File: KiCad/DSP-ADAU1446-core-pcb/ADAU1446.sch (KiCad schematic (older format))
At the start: 4 parts

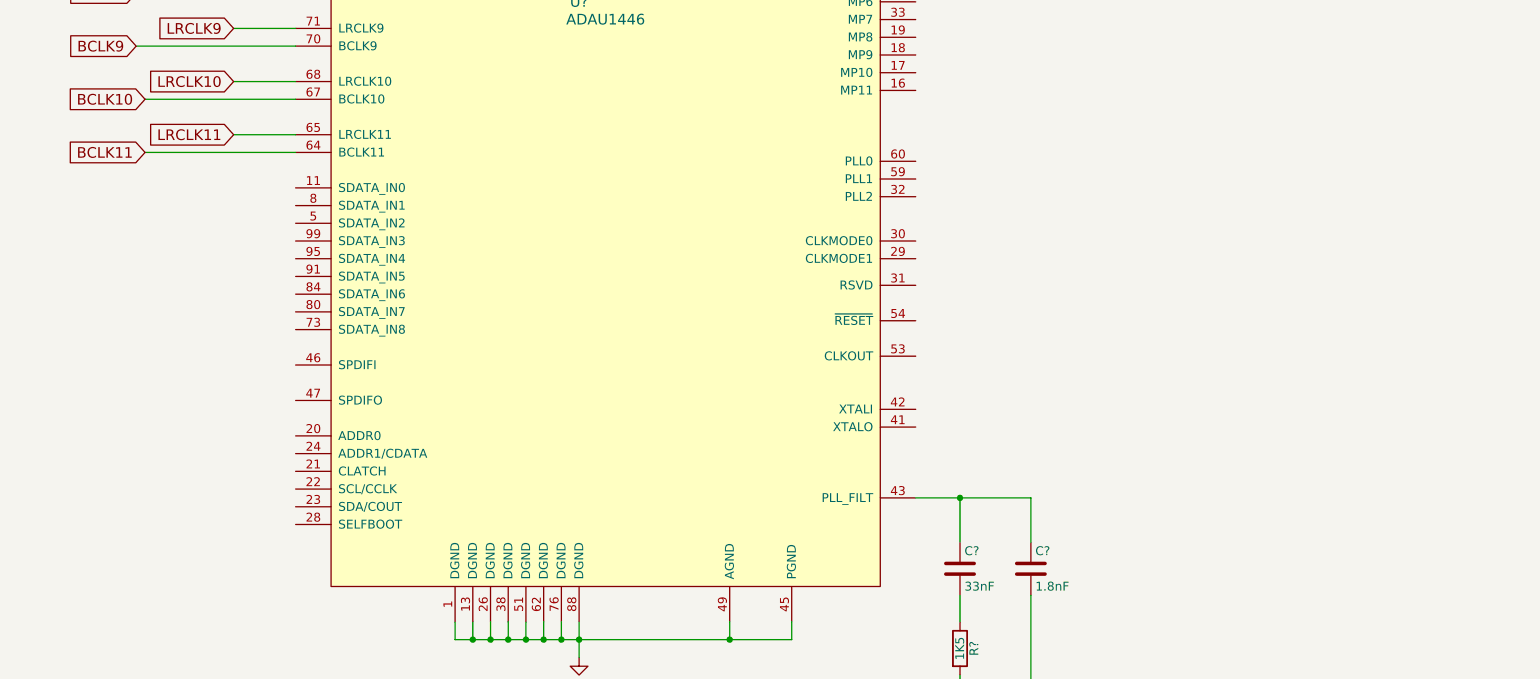
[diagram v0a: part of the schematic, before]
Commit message: - added switches library - updated ADAU1446 DSP core schematic
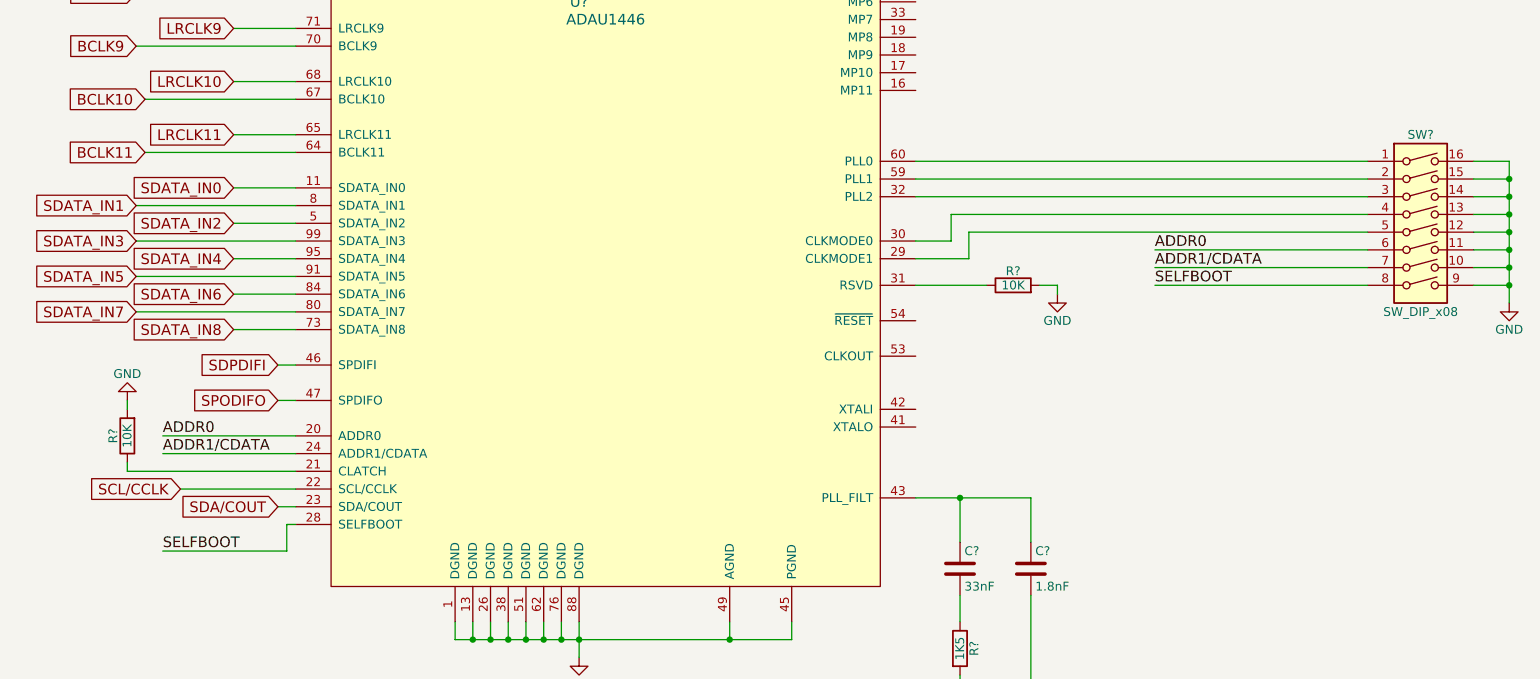
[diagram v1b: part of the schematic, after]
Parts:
- added R? (x2): 10K, symbol R
- added SW?: SW_DIP_x08, symbol SW_DIP_x08
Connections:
- net GND: now also R?.2, R?.2, SW?.10, SW?.11, SW?.12, SW?.13, SW?.14, SW?.15, SW?.16, SW?.9
- net SDATA_IN0: now reaches U?.11 (SDATA_IN0)
- net ADDR0: now reaches U?.20 (ADDR0)
- net ADDR0: now also SW?.6
- net at U?.21 (CLATCH): now also R?.1
- net SCL/CCLK: now reaches U?.22 (SCL/CCLK)
- net SDA/COUT: now reaches U?.23 (SDA/COUT)
- net ADDR1/CDATA: now reaches U?.24 (ADDR1/CDATA)
- net ADDR1/CDATA: now also SW?.7
- net SELFBOOT: now reaches U?.28 (SELFBOOT)
- net SELFBOOT: now also SW?.8
- net at U?.29 (CLKMODE1): now also SW?.5
- net at U?.30 (CLKMODE0): now also SW?.4
- net at U?.31 (RSVD): now also R?.1
- net at U?.32 (PLL2): now also SW?.3
- net SDPDIFI: now reaches U?.46 (SPDIFI)
- net SPODIFO: now reaches U?.47 (SPDIFO)
- net SDATA_IN2: now reaches U?.5 (SDATA_IN2)
- net at U?.59 (PLL1): now also SW?.2
- net at U?.60 (PLL0): now also SW?.1
- net SDATA_IN8: now reaches U?.73 (SDATA_IN8)
- net SDATA_IN1: now reaches U?.8 (SDATA_IN1)
- net SDATA_IN7: now reaches U?.80 (SDATA_IN7)
- net SDATA_IN6: now reaches U?.84 (SDATA_IN6)
- net SDATA_IN5: now reaches U?.91 (SDATA_IN5)
- net SDATA_IN4: now reaches U?.95 (SDATA_IN4)
- net SDATA_IN3: now reaches U?.99 (SDATA_IN3)
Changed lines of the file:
@@
 LIBS:valves
 LIBS:DSP-ADAU1446-core-pcb-cache
+LIBS:switches
 EELAYER 25 0
 EELAYER END
@@
 Wire Wire Line
 	10100 4300 9600 4300
+$Comp
+L SW_DIP_x08 SW?
+U 1 1 588F2B4E
+P 12450 6550
+F 0 "SW?" H 12450 7100 50  0000 C CNN
+F 1 "SW_DIP_x08" H 12450 6100 50  0000 C CNN
+F 2 "" H 12450 6550 50  0000 C CNN
+F 3 "" H 12450 6550 50  0000 C CNN
+	1    12450 6550
+	1    0    0    -1
+$EndComp
+$Comp
+L GND #PWR?
+U 1 1 588F2C1E
+P 12950 6950
+F 0 "#PWR?" H 12950 6700 50  0001 C CNN
+F 1 "GND" H 12950 6800 50  0000 C CNN
+F 2 "" H 12950 6950 50  0000 C CNN
+F 3 "" H 12950 6950 50  0000 C CNN
+	1    12950 6950
+	1    0    0    -1
+$EndComp
+Wire Wire Line
+	12750 6150 12950 6150
+Wire Wire Line
+	12950 6150 12950 6950
+Wire Wire Line
+	12750 6850 12950 6850
+Connection ~ 12950 6850
+Wire Wire Line
+	12750 6750 12950 6750
+Connection ~ 12950 6750
+Wire Wire Line
+	12750 6650 12950 6650
+Connection ~ 12950 6650
+Wire Wire Line
+	12750 6550 12950 6550
+Connection ~ 12950 6550
+Wire Wire Line
+	12750 6450 12950 6450
+Connection ~ 12950 6450
+Wire Wire Line
+	12750 6350 12950 6350
+Connection ~ 12950 6350
+Wire Wire Line
+	12750 6250 12950 6250
+Connection ~ 12950 6250
+Wire Wire Line
+	9600 6150 12150 6150
+Wire Wire Line
+	9600 6250 12150 6250
+Wire Wire Line
+	9600 6350 12150 6350
+Wire Wire Line
+	9600 6600 9800 6600
+Wire Wire Line
+	9800 6600 9800 6450
+Wire Wire Line
+	9800 6450 12150 6450
+Wire Wire Line
+	9600 6700 9900 6700
+Wire Wire Line
+	9900 6700 9900 6550
+Wire Wire Line
+	9900 6550 12150 6550
+Text Label 10950 6850 0    60   ~ 0
+SELFBOOT
+Wire Wire Line
+	10950 6850 12150 6850
+Text Label 10950 6650 0    60   ~ 0
+ADDR0
+Text Label 10950 6750 0    60   ~ 0
+ADDR1/CDATA
+Wire Wire Line
+	10950 6650 12150 6650
+Wire Wire Line
+	10950 6750 12150 6750
+Text Label 5350 7700 0    60   ~ 0
+ADDR0
+Text Label 5350 7800 0    60   ~ 0
+ADDR1/CDATA
+Text Label 5350 8350 0    60   ~ 0
+SELFBOOT
+Wire Wire Line
+	6100 7800 5350 7800
+Wire Wire Line
+	6100 7700 5350 7700
+$Comp
+L R R?
+U 1 1 588F383C
+P 10150 6850
+F 0 "R?" V 10230 6850 50  0000 C CNN
+F 1 "10K" V 10150 6850 50  0000 C CNN
+F 2 "" V 10080 6850 50  0000 C CNN
+F 3 "" H 10150 6850 50  0000 C CNN
+	1    10150 6850
+	0    -1   -1   0
+$EndComp
+Wire Wire Line
+	9600 6850 10000 6850
+$Comp
+L GND #PWR?
+U 1 1 588F3A17
+P 10400 6900
+F 0 "#PWR?" H 10400 6650 50  0001 C CNN
+F 1 "GND" H 10400 6750 50  0000 C CNN
+F 2 "" H 10400 6900 50  0000 C CNN
+F 3 "" H 10400 6900 50  0000 C CNN
+	1    10400 6900
+	1    0    0    -1
+$EndComp
+Wire Wire Line
+	10300 6850 10400 6850
+Wire Wire Line
+	10400 6850 10400 6900
+$Comp
+L R R?
+U 1 1 588F5B07
+P 5150 7700
+F 0 "R?" V 5230 7700 50  0000 C CNN
+F 1 "10K" V 5150 7700 50  0000 C CNN
+F 2 "" V 5080 7700 50  0000 C CNN
+F 3 "" H 5150 7700 50  0000 C CNN
+	1    5150 7700
+	-1   0    0    1
+$EndComp
+$Comp
+L GND #PWR?
+U 1 1 588F5B6E
+P 5150 7500
+F 0 "#PWR?" H 5150 7250 50  0001 C CNN
+F 1 "GND" H 5150 7350 50  0000 C CNN
+F 2 "" H 5150 7500 50  0000 C CNN
+F 3 "" H 5150 7500 50  0000 C CNN
+	1    5150 7500
+	-1   0    0    1
+$EndComp
+Wire Wire Line
+	5150 7900 6100 7900
+Text GLabel 5450 8000 0    60   Input ~ 0
+SCL/CCLK
+Text GLabel 6000 8100 0    60   Input ~ 0
+SDA/COUT
+Wire Wire Line
+	5350 8350 6050 8350
+Wire Wire Line
+	6050 8350 6050 8200
+Wire Wire Line
+	6050 8200 6100 8200
+Wire Wire Line
+	6000 8100 6100 8100
+Wire Wire Line
+	5450 8000 6100 8000
+Wire Wire Line
+	5150 7900 5150 7850
+Wire Wire Line
+	5150 7550 5150 7500
+Text GLabel 6000 7300 0    60   Input ~ 0
+SDPDIFI
+Text GLabel 6000 7500 0    60   Input ~ 0
+SPODIFO
+Wire Wire Line
+	6000 7300 6100 7300
+Wire Wire Line
+	6000 7500 6100 7500
+Text GLabel 5750 6300 0    60   Input ~ 0
+SDATA_IN0
+Text GLabel 5200 6400 0    60   Input ~ 0
+SDATA_IN1
+Text GLabel 5750 6500 0    60   Input ~ 0
+SDATA_IN2
+Text GLabel 5200 6600 0    60   Input ~ 0
+SDATA_IN3
+Text GLabel 5750 6700 0    60   Input ~ 0
+SDATA_IN4
+Text GLabel 5200 6800 0    60   Input ~ 0
+SDATA_IN5
+Text GLabel 5750 6900 0    60   Input ~ 0
+SDATA_IN6
+Text GLabel 5200 7000 0    60   Input ~ 0
+SDATA_IN7
+Text GLabel 5750 7100 0    60   Input ~ 0
+SDATA_IN8
+Wire Wire Line
+	5750 6300 6100 6300
+Wire Wire Line
+	6100 6400 5200 6400
+Wire Wire Line
+	6100 6500 5750 6500
+Wire Wire Line
+	6100 6600 5200 6600
+Wire Wire Line
+	5750 6700 6100 6700
+Wire Wire Line
+	6100 6800 5200 6800
+Wire Wire Line
+	6100 6900 5750 6900
+Wire Wire Line
+	6100 7000 5200 7000
+Wire Wire Line
+	6100 7100 5750 7100
 $EndSCHEMATC

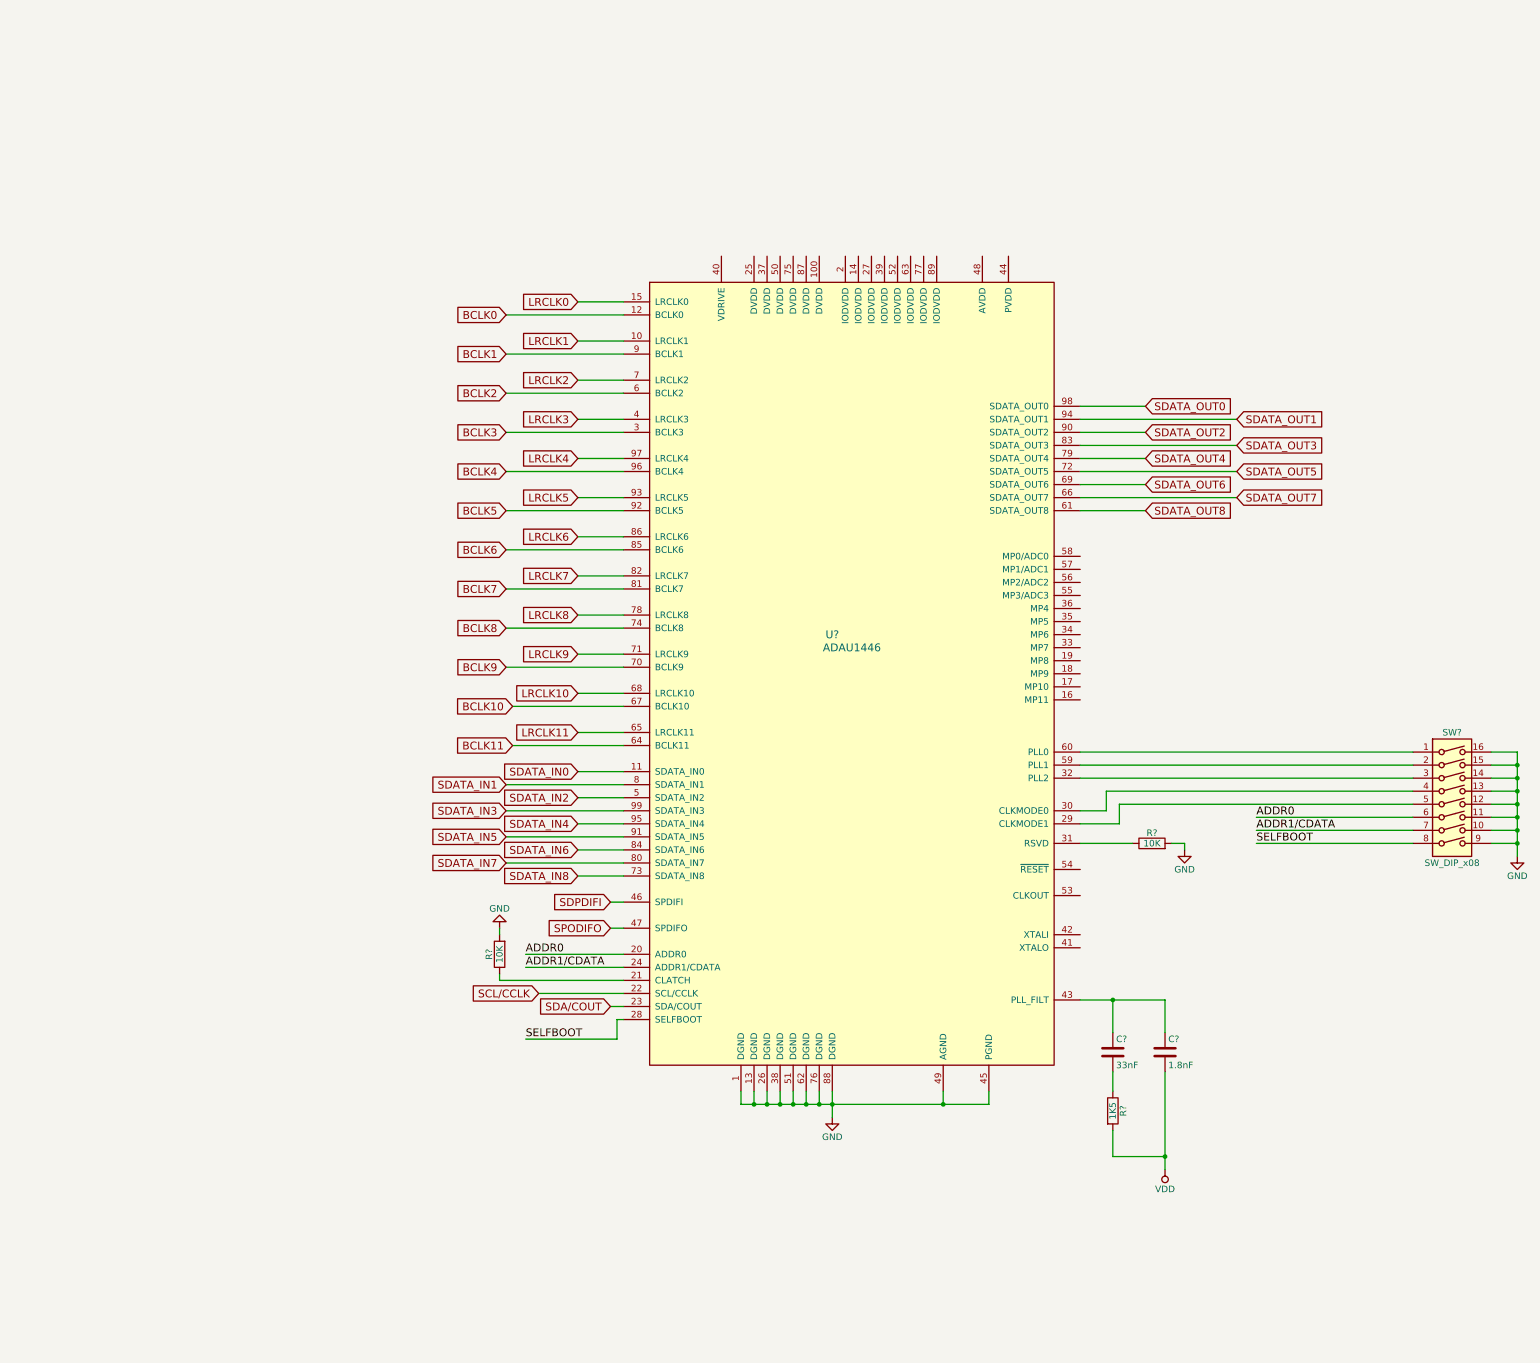
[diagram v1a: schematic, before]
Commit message: - finished schematics v0.1 - PCB work began - BOM generated
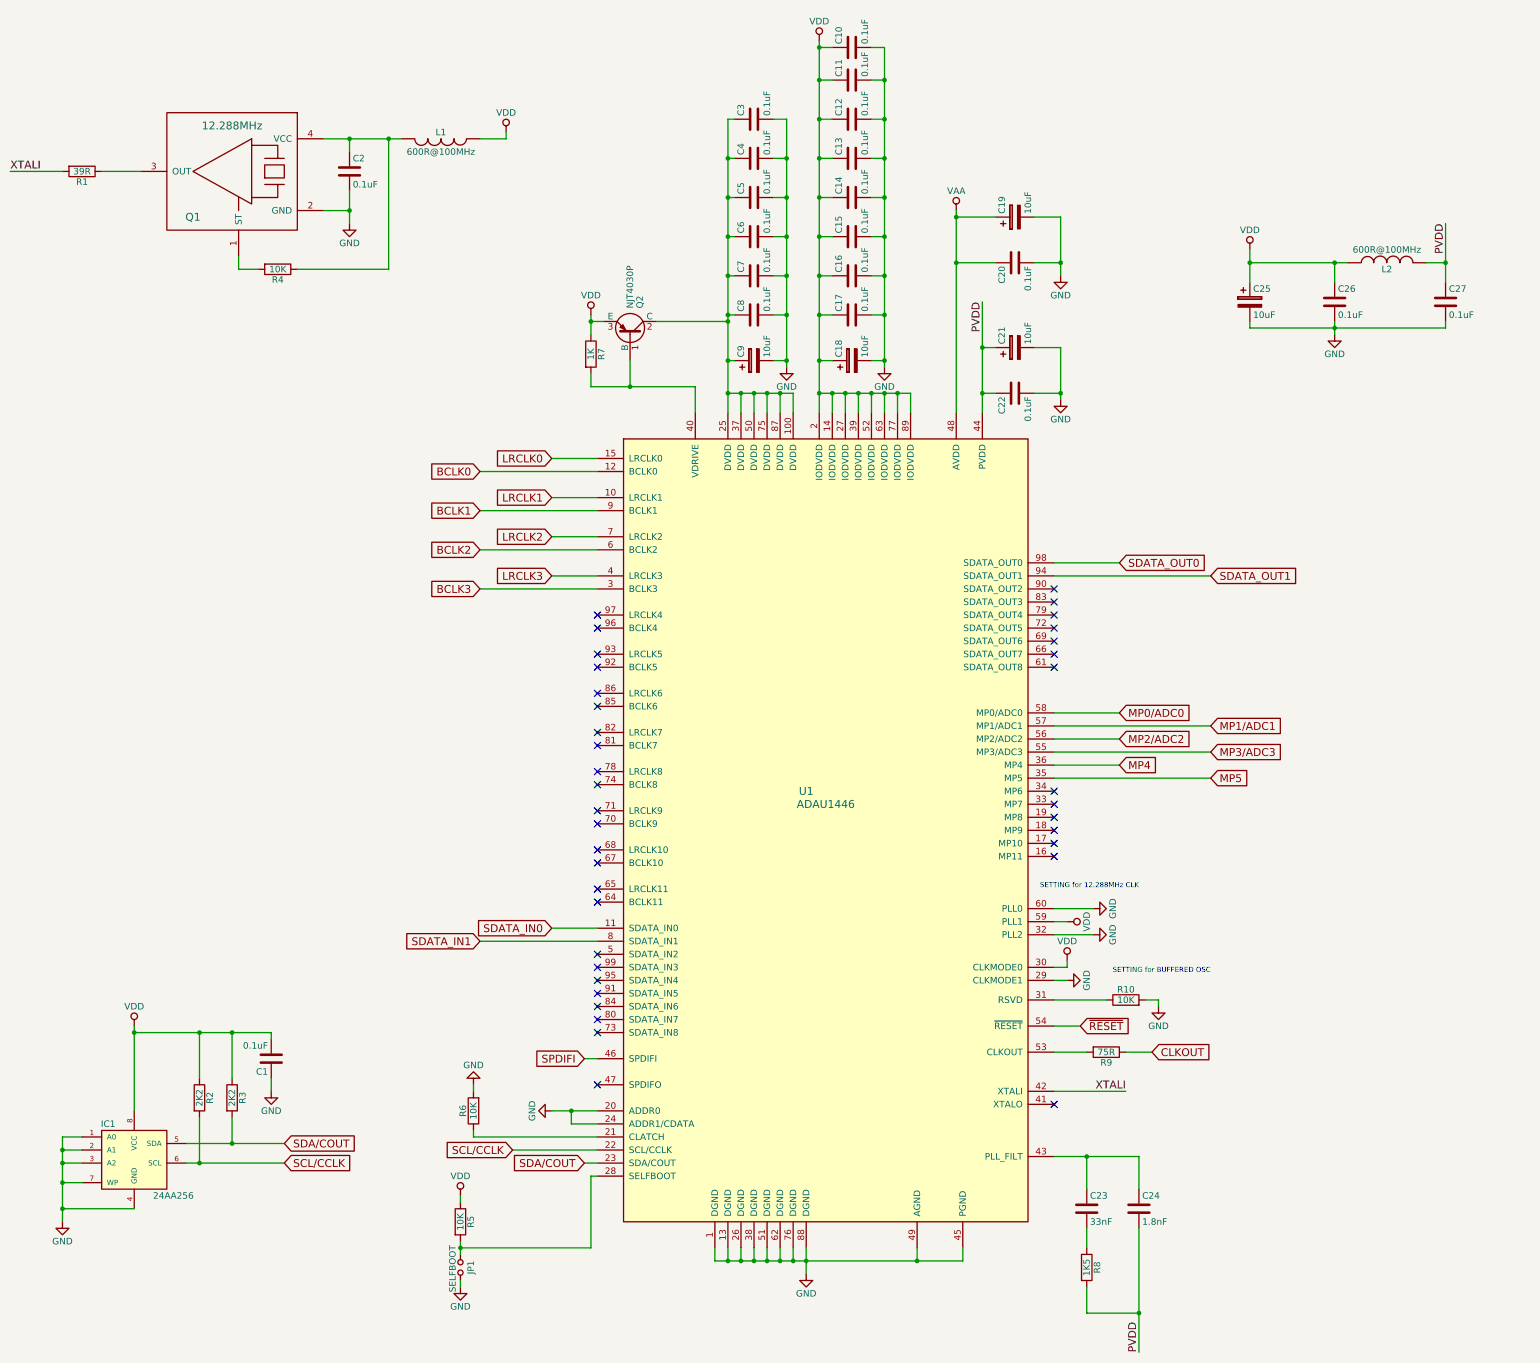
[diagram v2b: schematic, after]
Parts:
- removed SW?: SW_DIP_x08, symbol SW_DIP_x08
- removed U?: ADAU1446, symbol ADAU1446
- added C1, C10, C11, C12, C13, C14, C15, C16, C17, C2, C20, C22, C26, C27, C3, C4, C5, C6, C7, C8: 0.1uF, w_smd_cap:c_0603, symbol C
- added C18, C19, C21, C25, C9: 10uF, w_smd_cap:c_elec_4x5.3, symbol CP
- added IC1: 24AA256, w_smd_dil:msoic-8, symbol AT24CS02-SSHM
- added JP1: SELFBOOT, w_pin_strip:pin_socket_2, symbol Jumper_NO_Small
- added L1, L2: 600R@100MHz, w_smd_inductors:inductor_smd_0603, symbol INDUCTOR
- added Q1: 12.288MHz, w_crystal:crystal_epson, symbol EPSON_SG-210STF
- added Q2: NJT4030P, TO_SOT_Packages_SMD:SOT-223-3Lead_TabPin2, symbol BCP51
- added R1: 39R, w_smd_resistors:r_0603, symbol R
- added R2, R3: 2K2, w_smd_resistors:r_0603, symbol R
- added R4, R5: 10K, w_smd_resistors:r_0603, symbol R
- added R7: 1K, w_smd_resistors:r_0603, symbol R
- added R9: 75R, w_smd_resistors:r_0603, symbol R
- added U1: ADAU1446, w_smd_lqfp:TQFP-100, symbol ADAU1446
- C23, C24: renamed from C?; footprint (none) -> w_smd_cap:c_0603
- R10, R6, R8: renamed from R?; footprint (none) -> w_smd_resistors:r_0603
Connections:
- net BCLK0: now also U1.12 (BCLK0)
- net BCLK1: now also U1.9 (BCLK1)
- net BCLK2: now also U1.6 (BCLK2)
- net BCLK3: now also U1.3 (BCLK3)
- net GND: now also C1.1, C10.2, C11.2, C12.2, C13.2, C14.2, C15.2, C16.2, C17.2, C18.2, C19.2, C2.2, C20.2, C21.2, C22.2, C25.2, C26.2, C27.2, C3.2, C4.2, C5.2, C6.2, C7.2, C8.2, C9.2, IC1.1 (A0), IC1.2 (A1), IC1.3 (A2), IC1.4 (GND), IC1.7 (WP), JP1.2, Q1.2 (GND), U1.1 (DGND), U1.13 (DGND), U1.20 (ADDR0), U1.24 (ADDR1/CDATA), U1.26 (DGND), U1.29 (CLKMODE1), U1.32 (PLL2), U1.38 (DGND), U1.45 (PGND), U1.49 (AGND), U1.51 (DGND), U1.60 (PLL0), U1.62 (DGND), U1.76 (DGND), U1.88 (DGND)
- net LRCLK0: now also U1.15 (LRCLK0)
- net LRCLK1: now also U1.10 (LRCLK1)
- net LRCLK2: now also U1.7 (LRCLK2)
- net LRCLK3: now also U1.4 (LRCLK3)
- net SCL/CCLK: now also IC1.6 (SCL), R2.2, U1.22 (SCL/CCLK)
- net SDA/COUT: now also IC1.5 (SDA), R3.2, U1.23 (SDA/COUT)
- net SDATA_IN0: now also U1.11 (SDATA_IN0)
- net SDATA_IN1: now also U1.8 (SDATA_IN1)
- net SDATA_OUT0: now also U1.98 (SDATA_OUT0)
- net SDATA_OUT1: now also U1.94 (SDATA_OUT1)
- net VDD: now also C1.2, C10.1, C11.1, C12.1, C13.1, C14.1, C15.1, C16.1, C17.1, C18.1, C25.1, C26.1, IC1.8 (VCC), L1.1, L2.1, Q2.3 (E), R2.1, R3.1, R5.1, R7.1, U1.14 (IODVDD), U1.2 (IODVDD), U1.27 (IODVDD), U1.30 (CLKMODE0), U1.39 (IODVDD), U1.52 (IODVDD), U1.59 (PLL1), U1.63 (IODVDD), U1.77 (IODVDD), U1.89 (IODVDD); no longer C24.2, R8.2
- net at R6.1: now also U1.21 (CLATCH)
- net at R10.1: now also U1.31 (RSVD)
- net at C23.1, C24.1: now also U1.43 (PLL_FILT)
- new net: Q2.1 (B), R7.2, U1.40 (VDRIVE)
- new net: C3.1, C4.1, C5.1, C6.1, C7.1, C8.1, C9.1, Q2.2 (C), U1.100 (DVDD), U1.25 (DVDD), U1.37 (DVDD), U1.50 (DVDD), U1.75 (DVDD), U1.87 (DVDD)
- new net: R9.2, U1.53 (CLKOUT)
- new net: Q1.3 (OUT), R1.1
- new net: C2.1, L1.2, Q1.4 (VCC), R4.1
- new net: Q1.1 (ST), R4.2
- new net: JP1.1, R5.2, U1.28 (SELFBOOT)
- new net CLKOUT: R9.1
- new net MP0/ADC0: U1.58 (MP0/ADC0)
- new net MP1/ADC1: U1.57 (MP1/ADC1)
- new net MP2/ADC2: U1.56 (MP2/ADC2)
- new net MP3/ADC3: U1.55 (MP3/ADC3)
- new net MP4: U1.36 (MP4)
- new net MP5: U1.35 (MP5)
- new net PVDD: C21.1, C22.1, C24.2, C27.1, L2.2, R8.2, U1.44 (PVDD)
- new net SPDIFI: U1.46 (SPDIFI)
- new net VAA: C19.1, C20.1, U1.48 (AVDD)
- new net XTALI: R1.2, U1.42 (XTALI)
- new net ~RESET: U1.54 (~RESET)
- no-connect marks 0 -> 38
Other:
- note added: "SETTING for 12.288MHz CLK"
- note added: "SETTING for BUFFERED OSC"
- moved on the sheet: C23, C24, R10, R6, R8

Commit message: - modifyed regulator transistor
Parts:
- Q2: value NJT4030P -> FMMT734; footprint TO_SOT_Packages_SMD:SOT-223-3Lead_TabPin2 -> w_smd_trans:sot23
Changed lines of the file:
@@
 P 6150 2950
 F 0 "Q2" H 6350 3025 50  0000 L CNN
-F 1 "NJT4030P" H 6350 2950 50  0000 L CNN
-F 2 "TO_SOT_Packages_SMD:SOT-223-3Lead_TabPin2" H 6350 2875 50  0001 L CIN
+F 1 "FMMT734" H 6350 2950 50  0000 L CNN
+F 2 "w_smd_trans:sot23" H 6350 2875 50  0001 L CIN
 F 3 "" H 6150 2950 50  0000 L CNN
 	1    6150 2950

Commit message: -pcb update - changed footprint of IC1 and U2 to SO8
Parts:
- IC1: footprint w_smd_dil:msoic-8 -> w_smd_dil:so-8
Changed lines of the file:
@@
 F 0 "IC1" H 2150 9500 50  0000 C CNN
 F 1 "24AA256" H 2650 8950 50  0000 C CNN
-F 2 "w_smd_dil:msoic-8" H 2350 9250 50  0001 C CIN
+F 2 "w_smd_dil:so-8" H 2350 9250 50  0001 C CIN
 F 3 "" H 2350 9250 50  0000 C CNN
 	1    2350 9250
